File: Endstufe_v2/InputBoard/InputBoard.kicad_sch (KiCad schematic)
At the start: 11 parts, among them J11 DNP, J5 B4B-XH-2_(LF)(SN), J6 B4B-XH-2_(LF)(SN), J7 B4B-XH-2_(LF)(SN), J8 Conn_01x02_Pin, J9 B4B-XH-2_(LF)(SN)

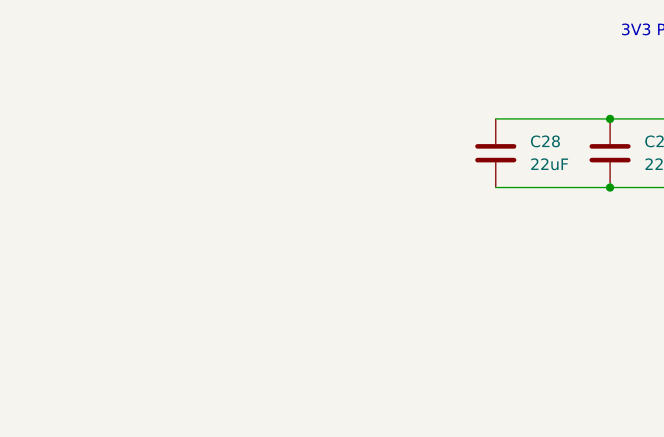
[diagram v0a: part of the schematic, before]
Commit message: Continue working on input board and use ADAU1467 instaed of ADAU1463
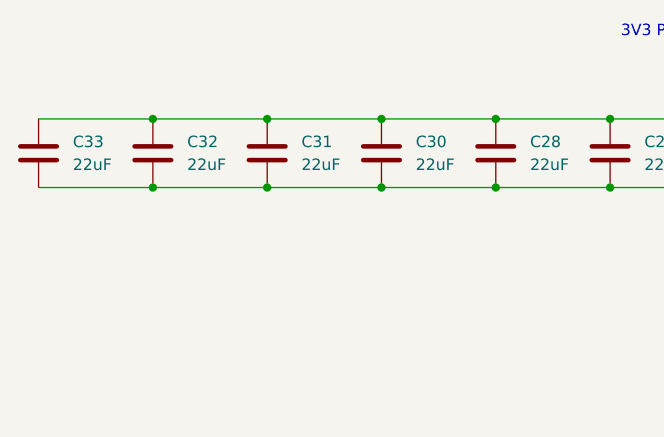
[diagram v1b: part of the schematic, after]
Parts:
- added C30, C31, C32, C33: 22uF, Endstufe:C_0603_1608Metric, symbol Endstufe:C
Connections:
- net +3V3: now also C30.1, C31.1, C32.1, C33.1
- net GND: now also C30.2, C31.2, C32.2, C33.2

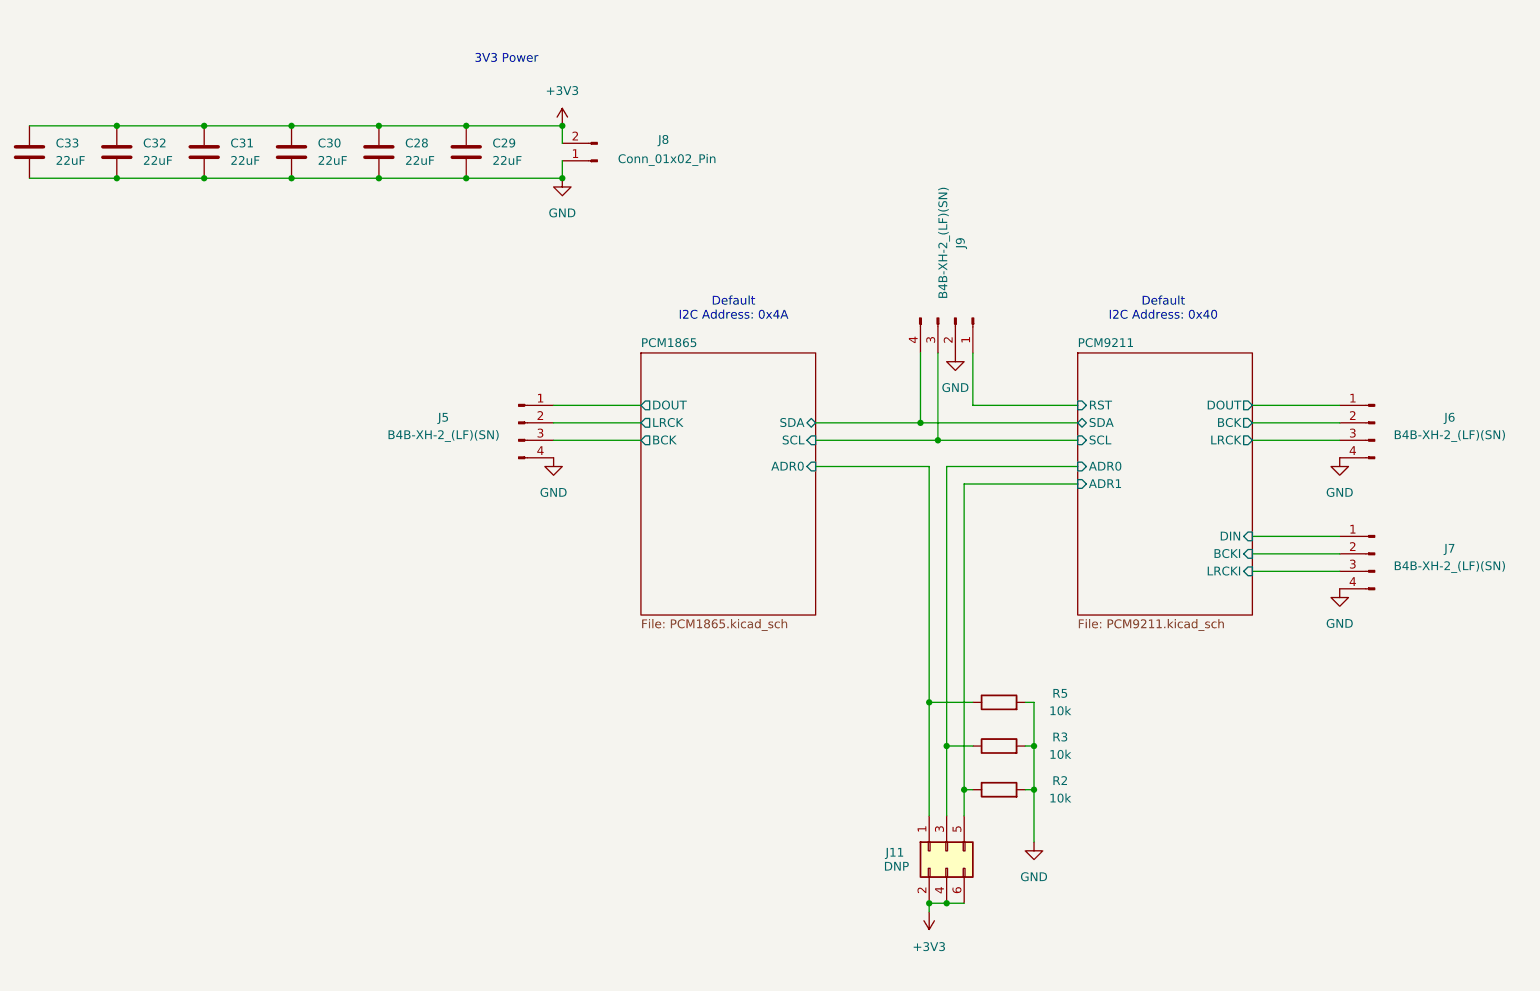
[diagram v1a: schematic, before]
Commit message: Make mounting holes and continue layouting
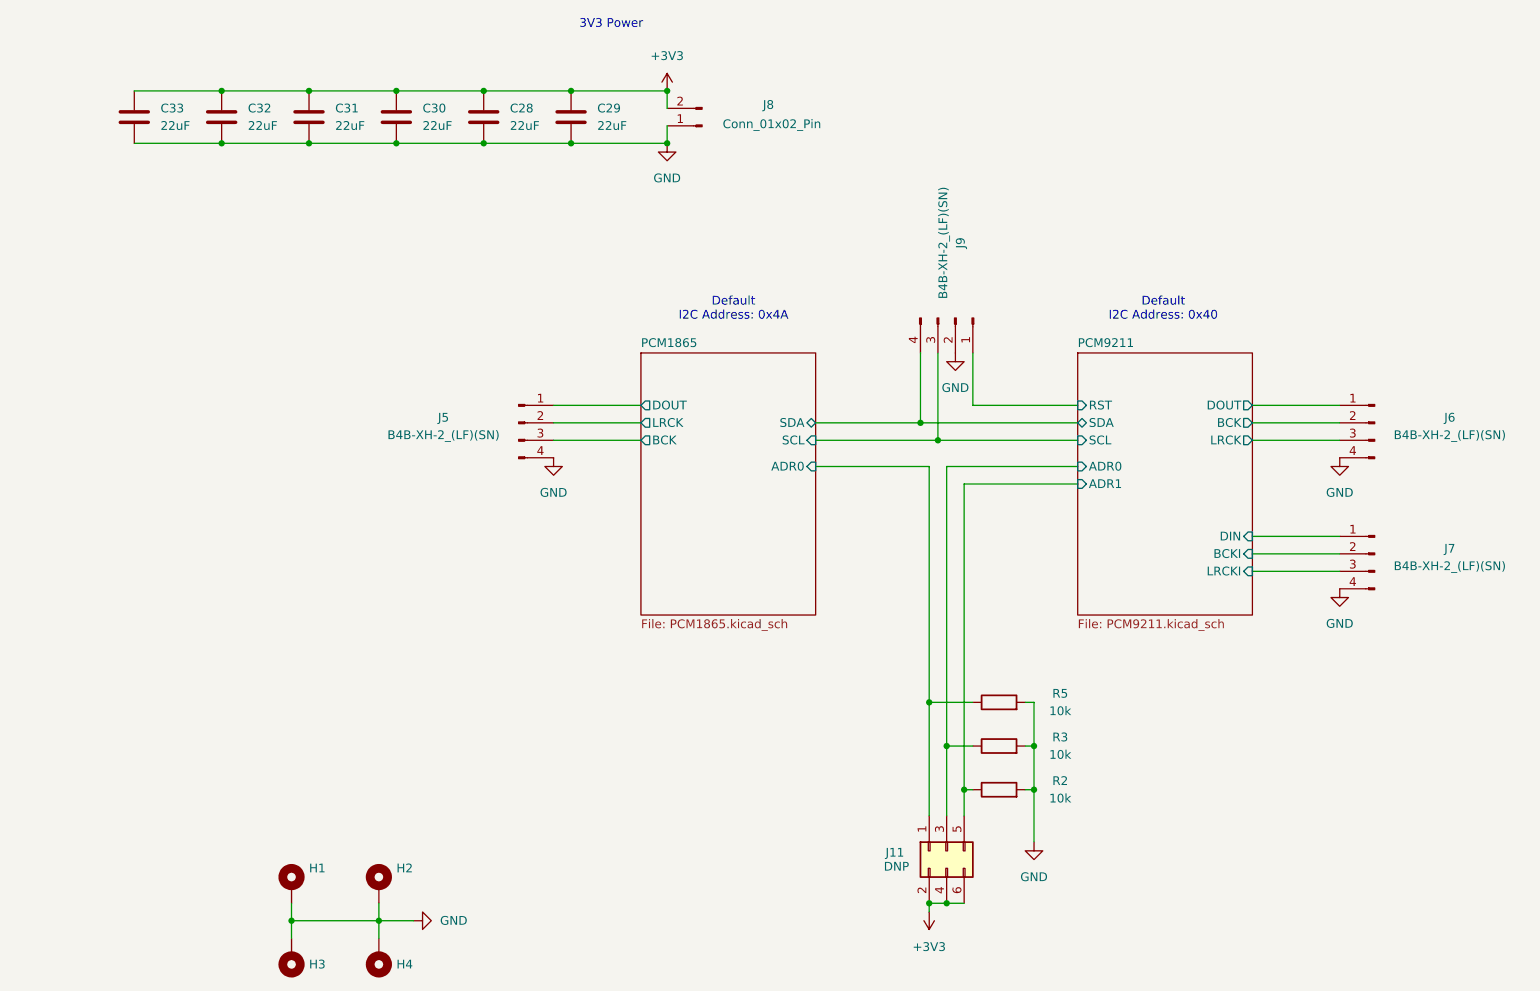
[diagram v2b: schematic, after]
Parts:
- added H1, H2, H3, H4: MountingHole_Pad, Endstufe:MountingHole_3.2mm_M3_ISO14580_Pad, symbol Endstufe:MountingHole_Pad
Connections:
- net GND: now also H1.1, H2.1, H3.1, H4.1
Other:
- moved on the sheet: C28, C29, C30, C31, C32, C33, J8

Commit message: Change unavailable parts to available ones, optimise silkscreen, do via stiching
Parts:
- J5, J6, J7, J9: footprint Endstufe:CONN-TH_B4B-XH-2-LF-SN -> Endstufe:JST_XH_B4B-XH-A_1x04_P2.50mm_Vertical; JLCPCB Position Offset (none) -> 0,-0.5
- J8: footprint Connector_JST:JST_XH_B2B-XH-A_1x02_P2.50mm_Vertical -> Endstufe:JST_XH_B2B-XH-A_1x02_P2.50mm_Vertical; JLCPCB Position Offset (none) -> 0,-0.5; LCSC (none) -> C158012
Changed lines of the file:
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@@
 			)
 		)
-		(property "Footprint" "Endstufe:CONN-TH_B4B-XH-2-LF-SN"
+		(property "Footprint" "Endstufe:JST_XH_B4B-XH-A_1x04_P2.50mm_Vertical"
 			(at 83.82 96.52 0)
 			(effects
@@
 		(property "LCSC" "C157999"
 			(at 84.074 103.886 0)
+			(effects
+				(font
+					(size 1.27 1.27)
+				)
+				(hide yes)
+			)
+		)
+		(property "JLCPCB Position Offset" "0,-0.5"
+			(at 0 172.72 0)
 			(effects
 				(font
@@
 			)
 		)
-		(property "Footprint" "Endstufe:CONN-TH_B4B-XH-2-LF-SN"
+		(property "Footprint" "Endstufe:JST_XH_B4B-XH-A_1x04_P2.50mm_Vertical"
 			(at 208.28 115.57 0)
 			(effects
@@
 			)
 		)
+		(property "JLCPCB Position Offset" "0,-0.5"
+			(at 416.56 210.82 0)
+			(effects
+				(font
+					(size 1.27 1.27)
+				)
+				(hide yes)
+			)
+		)
 		(pin "4"
 		)
@@
 			)
 		)
-		(property "Footprint" "Endstufe:CONN-TH_B4B-XH-2-LF-SN"
+		(property "Footprint" "Endstufe:JST_XH_B4B-XH-A_1x04_P2.50mm_Vertical"
 			(at 137.16 71.12 0)
 			(effects
@@
 		(property "LCSC" "C157999"
 			(at 129.794 71.374 0)
+			(effects
+				(font
+					(size 1.27 1.27)
+				)
+				(hide yes)
+			)
+		)
+		(property "JLCPCB Position Offset" "0,-0.5"
+			(at 76.2 -76.2 0)
 			(effects
 				(font
@@
 			)
 		)
-		(property "Footprint" "Endstufe:CONN-TH_B4B-XH-2-LF-SN"
+		(property "Footprint" "Endstufe:JST_XH_B4B-XH-A_1x04_P2.50mm_Vertical"
 			(at 208.28 96.52 0)
 			(effects
@@
 		(property "LCSC" "C157999"
 			(at 208.026 103.886 0)
+			(effects
+				(font
+					(size 1.27 1.27)
+				)
+				(hide yes)
+			)
+		)
+		(property "JLCPCB Position Offset" "0,-0.5"
+			(at 416.56 172.72 0)
 			(effects
 				(font
@@
 			)
 		)
-		(property "Footprint" "Connector_JST:JST_XH_B2B-XH-A_1x02_P2.50mm_Vertical"
+		(property "Footprint" "Endstufe:JST_XH_B2B-XH-A_1x02_P2.50mm_Vertical"
 			(at 110.49 43.18 0)
 			(effects
@@
 			(effects
 				(font
+					(size 1.27 1.27)
+				)
+				(hide yes)
+			)
+		)
+		(property "JLCPCB Position Offset" "0,-0.5"
+			(at 220.98 0 0)
+			(effects
+				(font
+					(size 1.27 1.27)
+				)
+				(hide yes)
+			)
+		)
+		(property "LCSC" "C158012"
+			(at 220.98 0 0)
+			(effects
+				(font
